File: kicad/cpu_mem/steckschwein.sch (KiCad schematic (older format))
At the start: 28 parts, among them P1 CONN_02X04, P3 CONN_01X03, P4 CONN_02X02, SW1 SW_PUSH, U1 W65C02SP, U2 LM555N, U3 74HCT00, U4 74LS393, U6 28C256, U7 HM62256BLP-7, U8 HM62256BLP-7, X1 OSC

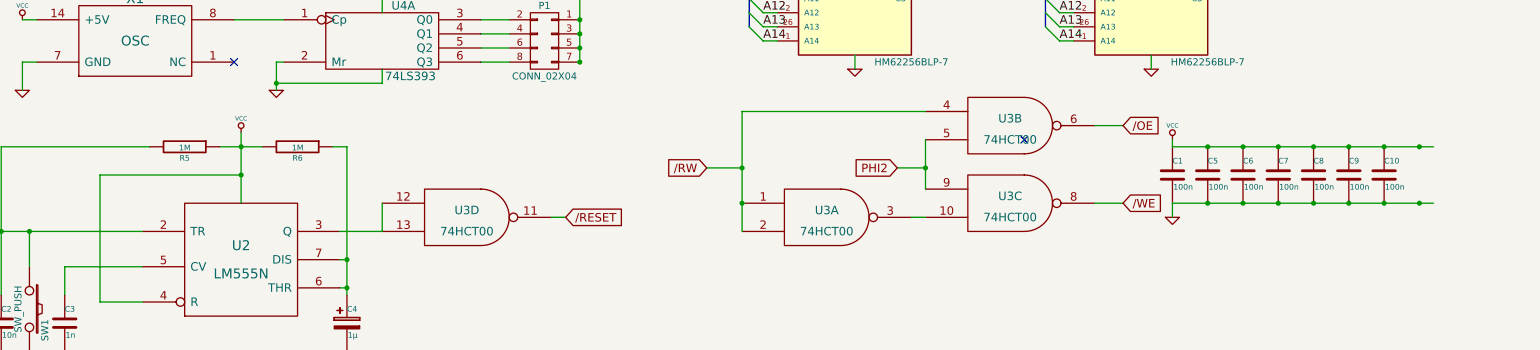
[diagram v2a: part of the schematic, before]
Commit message: memctl register auslesbar
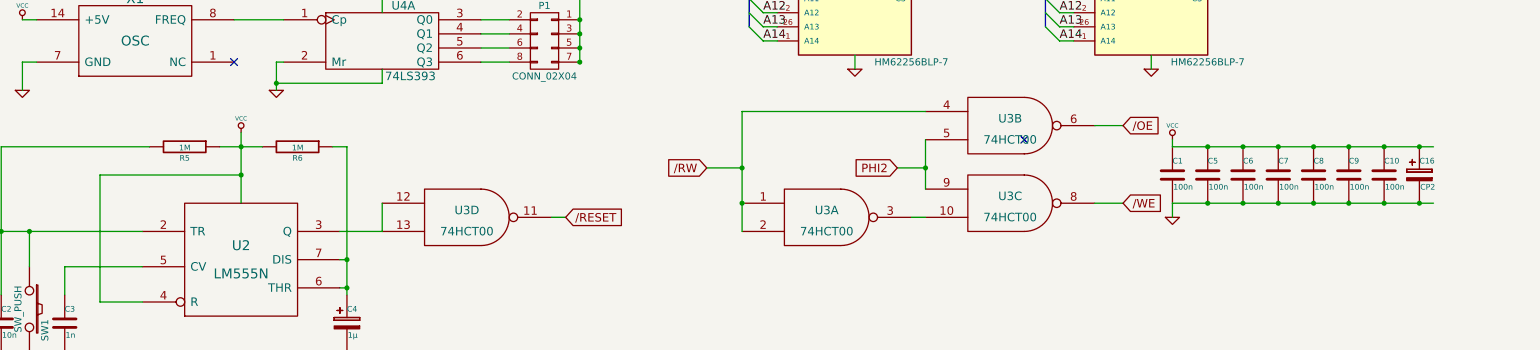
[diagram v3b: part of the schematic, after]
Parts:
- added C16: CP2, Capacitors_Elko_ThroughHole:Elko_vert_11.2x7.5mm_RM2.5, symbol CP2
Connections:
- net GND: now also C16.2
- net VCC: now also C16.1
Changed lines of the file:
@@
 LIBS:74xgxx
 LIBS:ttl_ieee
+LIBS:steckschwein-cache
 EELAYER 24 0
 EELAYER END
@@
 $EndComp
 $Comp
-L VCC #PWR20
+L VCC #PWR01
 U 1 1 5413678B
 P 8900 5600
-F 0 "#PWR20" H 8900 5700 30  0001 C CNN
+F 0 "#PWR01" H 8900 5700 30  0001 C CNN
 F 1 "VCC" H 8900 5700 30  0000 C CNN
 F 2 "" H 8900 5600 60  0000 C CNN
@@
 $EndComp
 $Comp
-L GND #PWR21
+L GND #PWR02
 U 1 1 541367AD
 P 8900 6150
-F 0 "#PWR21" H 8900 6150 30  0001 C CNN
+F 0 "#PWR02" H 8900 6150 30  0001 C CNN
 F 1 "GND" H 8900 6080 30  0001 C CNN
 F 2 "" H 8900 6150 60  0000 C CNN
@@
 $EndComp
 $Comp
-L VCC #PWR6
+L VCC #PWR03
 U 1 1 54136970
 P 2750 2700
-F 0 "#PWR6" H 2750 2800 30  0001 C CNN
+F 0 "#PWR03" H 2750 2800 30  0001 C CNN
 F 1 "VCC" H 2750 2800 30  0000 C CNN
 F 2 "" H 2750 2700 60  0000 C CNN
@@
 $EndComp
 $Comp
-L GND #PWR7
+L GND #PWR04
 U 1 1 541369C9
 P 2750 3250
-F 0 "#PWR7" H 2750 3250 30  0001 C CNN
+F 0 "#PWR04" H 2750 3250 30  0001 C CNN
 F 1 "GND" H 2750 3180 30  0001 C CNN
 F 2 "" H 2750 3250 60  0000 C CNN
@@
 $EndComp
 $Comp
-L VCC #PWR4
+L VCC #PWR05
 U 1 1 54136DD8
 P 2300 5550
-F 0 "#PWR4" H 2300 5650 30  0001 C CNN
+F 0 "#PWR05" H 2300 5650 30  0001 C CNN
 F 1 "VCC" H 2300 5650 30  0000 C CNN
 F 2 "" H 2300 5550 60  0000 C CNN
@@
 $EndComp
 $Comp
-L GND #PWR8
+L GND #PWR06
 U 1 1 541371BF
 P 3050 7400
-F 0 "#PWR8" H 3050 7400 30  0001 C CNN
+F 0 "#PWR06" H 3050 7400 30  0001 C CNN
 F 1 "GND" H 3050 7330 30  0001 C CNN
 F 2 "" H 3050 7400 60  0000 C CNN
@@
 $EndComp
 $Comp
-L VCC #PWR1
+L VCC #PWR07
 U 1 1 5413551C
 P 550 3350
-F 0 "#PWR1" H 550 3450 30  0001 C CNN
+F 0 "#PWR07" H 550 3450 30  0001 C CNN
 F 1 "VCC" H 550 3450 30  0000 C CNN
 F 2 "" H 550 3350 60  0000 C CNN
@@
 $EndComp
 $Comp
-L VCC #PWR11
+L VCC #PWR08
 U 1 1 5413558F
 P 3750 3550
-F 0 "#PWR11" H 3750 3650 30  0001 C CNN
+F 0 "#PWR08" H 3750 3650 30  0001 C CNN
 F 1 "VCC" H 3750 3650 30  0000 C CNN
 F 2 "" H 3750 3550 60  0000 C CNN
@@
 $EndComp
 $Comp
-L VCC #PWR2
+L VCC #PWR09
 U 1 1 54136377
 P 750 4750
-F 0 "#PWR2" H 750 4850 30  0001 C CNN
+F 0 "#PWR09" H 750 4850 30  0001 C CNN
 F 1 "VCC" H 750 4850 30  0000 C CNN
 F 2 "" H 750 4750 60  0000 C CNN
@@
 $EndComp
 $Comp
-L GND #PWR3
+L GND #PWR010
 U 1 1 541363D2
 P 750 5250
-F 0 "#PWR3" H 750 5250 30  0001 C CNN
+F 0 "#PWR010" H 750 5250 30  0001 C CNN
 F 1 "GND" H 750 5180 30  0001 C CNN
 F 2 "" H 750 5250 60  0000 C CNN
@@
 $EndComp
 $Comp
-L GND #PWR5
+L GND #PWR011
 U 1 1 5413653F
 P 2550 5250
-F 0 "#PWR5" H 2550 5250 30  0001 C CNN
+F 0 "#PWR011" H 2550 5250 30  0001 C CNN
 F 1 "GND" H 2550 5180 30  0001 C CNN
 F 2 "" H 2550 5250 60  0000 C CNN
@@
 $EndComp
 $Comp
-L VCC #PWR9
+L VCC #PWR012
 U 1 1 5413674B
 P 3300 4550
-F 0 "#PWR9" H 3300 4650 30  0001 C CNN
+F 0 "#PWR012" H 3300 4650 30  0001 C CNN
 F 1 "VCC" H 3300 4650 30  0000 C CNN
 F 2 "" H 3300 4550 60  0000 C CNN
@@
 $EndComp
 $Comp
-L VCC #PWR14
+L VCC #PWR013
 U 1 1 5413EA26
 P 7000 2550
-F 0 "#PWR14" H 7000 2650 30  0001 C CNN
+F 0 "#PWR013" H 7000 2650 30  0001 C CNN
 F 1 "VCC" H 7000 2650 30  0000 C CNN
 F 2 "" H 7000 2550 60  0000 C CNN
@@
 $EndComp
 $Comp
-L GND #PWR10
+L GND #PWR014
 U 1 1 5414A44F
 P 3400 3450
-F 0 "#PWR10" H 3400 3450 30  0001 C CNN
+F 0 "#PWR014" H 3400 3450 30  0001 C CNN
 F 1 "GND" H 3400 3380 30  0001 C CNN
 F 2 "" H 3400 3450 60  0000 C CNN
@@
 A5
 $Comp
-L VCC #PWR16
+L VCC #PWR015
 U 1 1 543745A2
 P 8100 700
-F 0 "#PWR16" H 8100 800 30  0001 C CNN
+F 0 "#PWR015" H 8100 800 30  0001 C CNN
 F 1 "VCC" H 8100 800 30  0000 C CNN
 F 2 "" H 8100 700 60  0000 C CNN
@@
 $EndComp
 $Comp
-L GND #PWR17
+L GND #PWR016
 U 1 1 543748B3
 P 8100 3000
-F 0 "#PWR17" H 8100 3000 30  0001 C CNN
+F 0 "#PWR016" H 8100 3000 30  0001 C CNN
 F 1 "GND" H 8100 2930 30  0001 C CNN
 F 2 "" H 8100 3000 60  0000 C CNN
@@
 $EndComp
 $Comp
-L VCC #PWR12
+L VCC #PWR017
 U 1 1 54374D46
 P 6650 3300
-F 0 "#PWR12" H 6650 3400 30  0001 C CNN
+F 0 "#PWR017" H 6650 3400 30  0001 C CNN
 F 1 "VCC" H 6650 3400 30  0000 C CNN
 F 2 "" H 6650 3300 60  0000 C CNN
@@
 $EndComp
 $Comp
-L VCC #PWR18
+L VCC #PWR018
 U 1 1 54374E0E
 P 8750 3300
-F 0 "#PWR18" H 8750 3400 30  0001 C CNN
+F 0 "#PWR018" H 8750 3400 30  0001 C CNN
 F 1 "VCC" H 8750 3400 30  0000 C CNN
 F 2 "" H 8750 3300 60  0000 C CNN
@@
 $EndComp
 $Comp
-L GND #PWR13
+L GND #PWR019
 U 1 1 54375105
 P 6650 5100
-F 0 "#PWR13" H 6650 5100 30  0001 C CNN
+F 0 "#PWR019" H 6650 5100 30  0001 C CNN
 F 1 "GND" H 6650 5030 30  0001 C CNN
 F 2 "" H 6650 5100 60  0000 C CNN
@@
 $EndComp
 $Comp
-L GND #PWR19
+L GND #PWR020
 U 1 1 54375267
 P 8750 5100
-F 0 "#PWR19" H 8750 5100 30  0001 C CNN
+F 0 "#PWR020" H 8750 5100 30  0001 C CNN
 F 1 "GND" H 8750 5030 30  0001 C CNN
 F 2 "" H 8750 5100 60  0000 C CNN
@@
 	1300 6750 1300 5850
 Wire Wire Line
-	1300 5850 2300 5850
+	2300 5850 1300 5850
 Connection ~ 2300 5850
 Wire Wire Line
@@
 Wire Wire Line
 	6100 1950 4850 1950
+$Comp
+L CP2 C16
+U 1 1 546AA0E1
+P 10650 5850
+F 0 "C16" H 10650 5950 40  0000 L CNN
+F 1 "CP2" H 10656 5765 40  0000 L CNN
+F 2 "Capacitors_Elko_ThroughHole:Elko_vert_11.2x7.5mm_RM2.5" H 10688 5700 30  0001 C CNN
+F 3 "" H 10650 5850 60  0000 C CNN
+	1    10650 5850
+	1    0    0    -1
+$EndComp
 $EndSCHEMATC

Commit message: update
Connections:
- net /CS_ROM: now also U6.20 (CS)
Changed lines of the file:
@@
 LIBS:ttl_ieee
 LIBS:steckschwein-cache
-EELAYER 24 0
+EELAYER 25 0
 EELAYER END
 $Descr A4 11693 8268
@@
 	1300 6750 1300 5850
 Wire Wire Line
-	2300 5850 1300 5850
+	1300 5850 2300 5850
 Connection ~ 2300 5850
 Wire Wire Line
@@
 Wire Wire Line
 	7400 2750 7200 2750
-Wire Wire Line
-	7400 2850 7200 2850
 Wire Bus Line
 	9050 750  9050 1650
@@
 Text Label 9450 4600 0    60   ~ 0
 /CS_HIRAM
-Text Label 7000 2950 0    60   ~ 0
-/CS_ROM
-Wire Wire Line
-	4850 800  5150 800
 Wire Wire Line
 	4850 900  5150 900
 Wire Wire Line
 	4850 1000 5150 1000
-Text Label 5100 800  0    60   ~ 0
-/CS_ROM
 Text Label 5100 900  0    60   ~ 0
 /CS_LORAM
@@
 	1    0    0    -1
 $EndComp
+Wire Wire Line
+	6300 2850 7400 2850
+Text Label 6950 2950 0    60   ~ 0
+/CS_ROM
+Wire Wire Line
+	4850 800  6300 800
+Text Label 5150 800  0    60   ~ 0
+/CS_ROM
+Wire Wire Line
+	6300 800  6300 2850
 $EndSCHEMATC

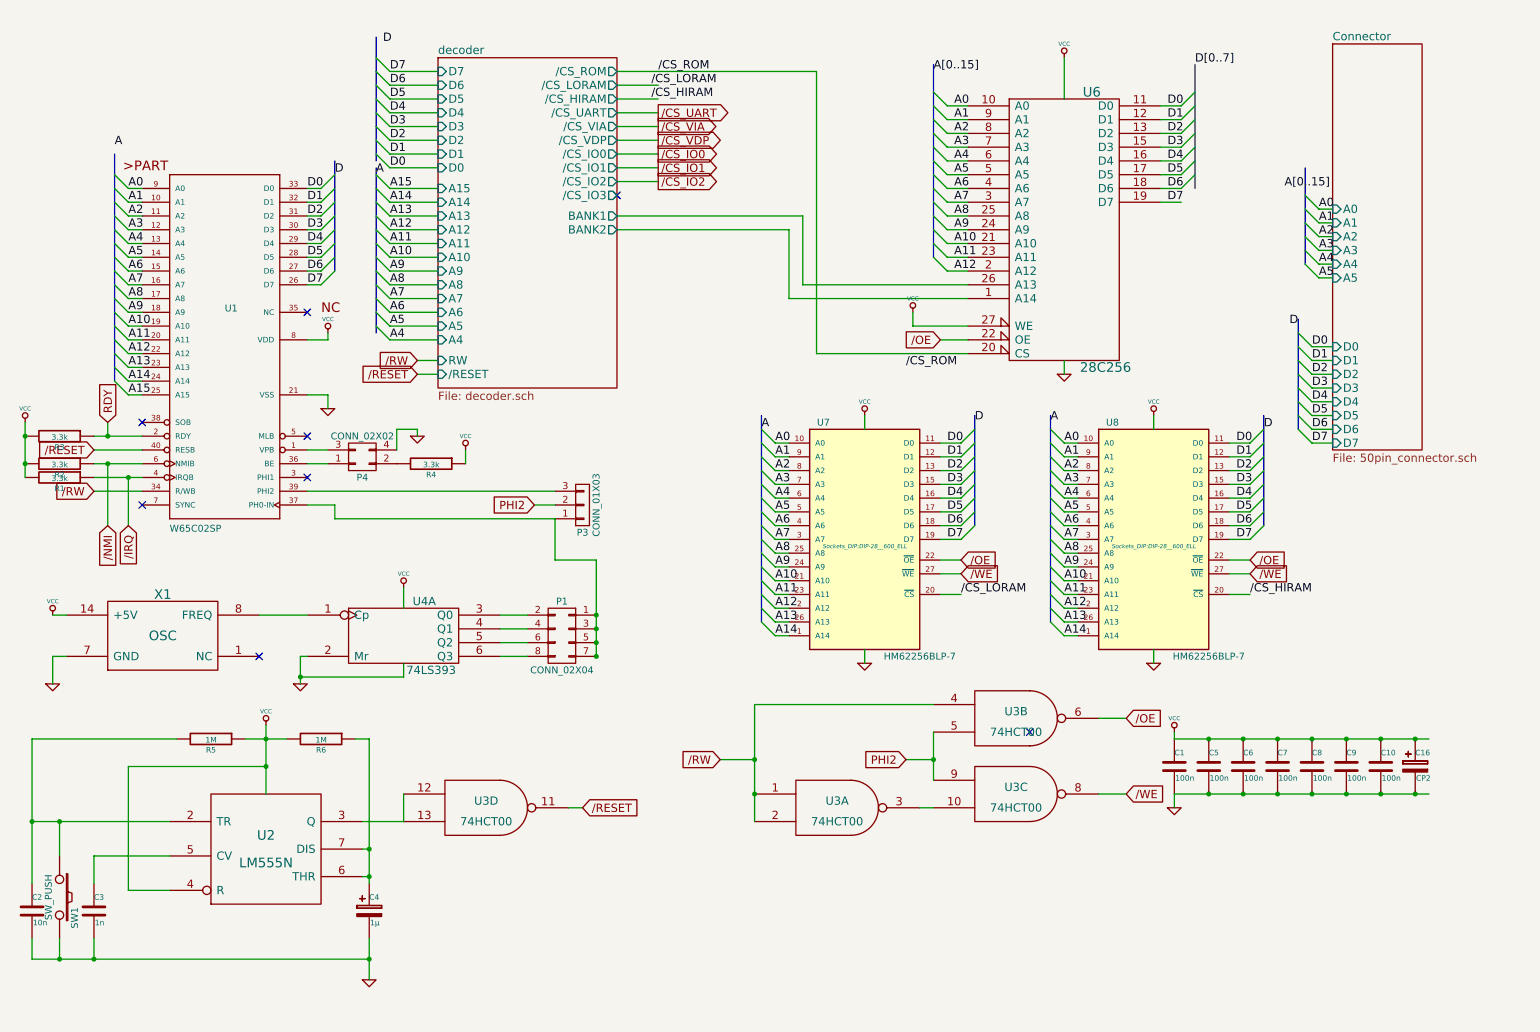
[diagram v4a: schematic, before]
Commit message: anpassungen latch, decoder, 2. unit 393 inputs auf masse
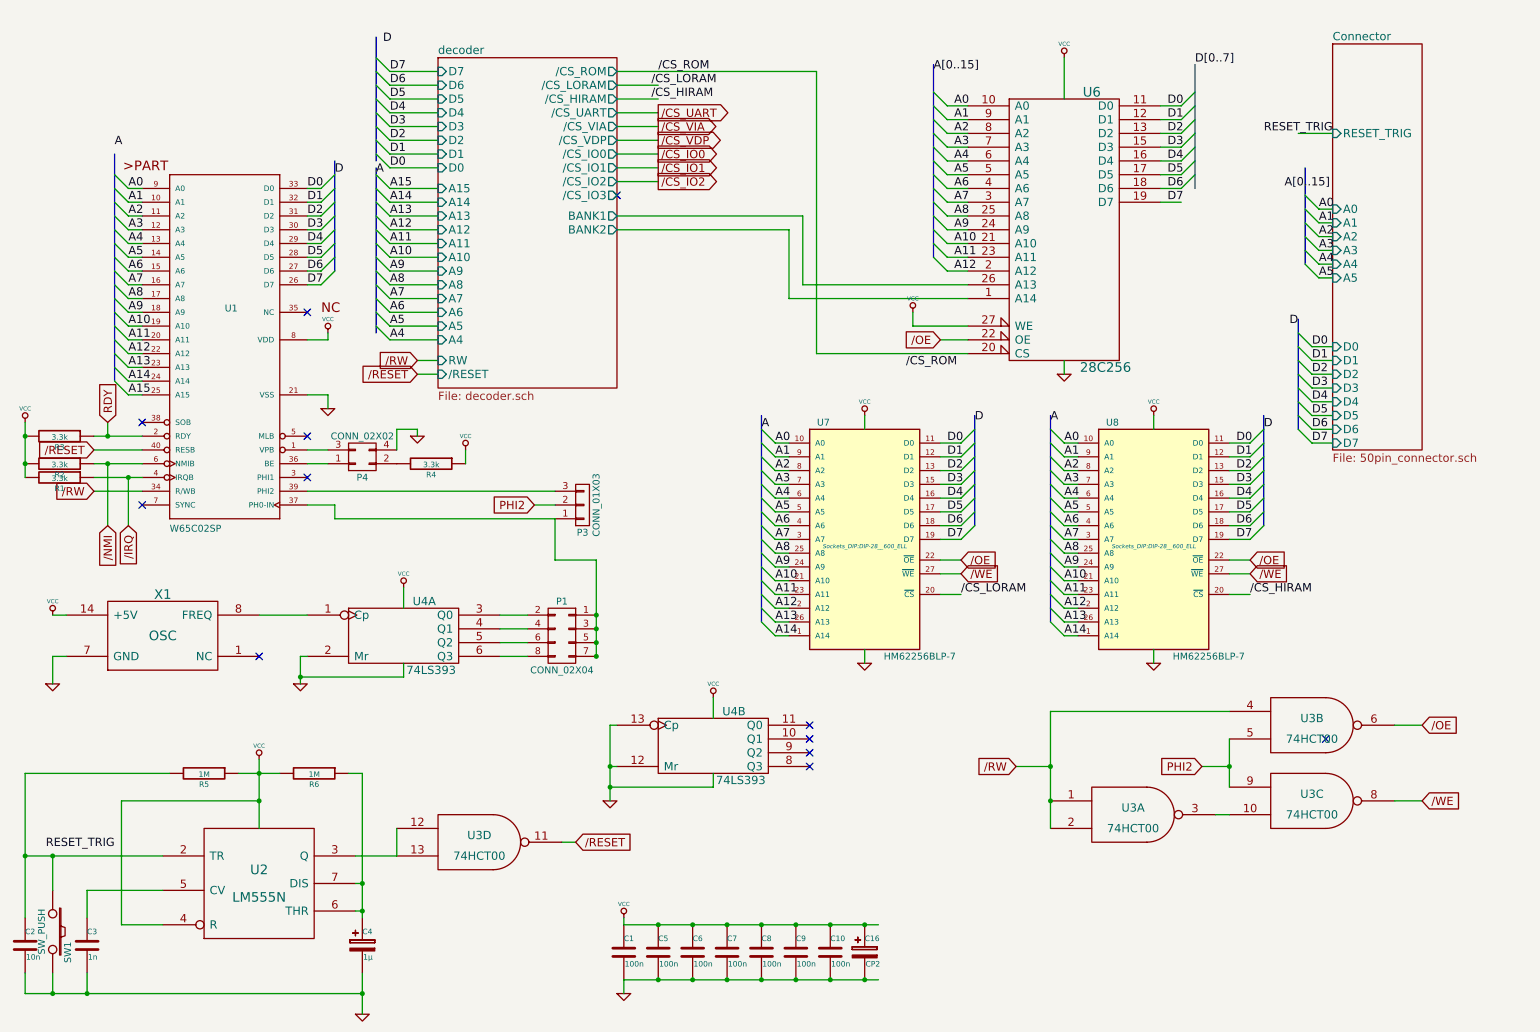
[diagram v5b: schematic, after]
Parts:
- added unit 2 of U4
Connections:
- net GND: now also U4.12 (Mr), U4.13 (Cp), U4.7 (GND)
- net VCC: now also U4.14 (VCC)
- no-connect marks 8 -> 12
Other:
- moved on the sheet: C1, C10, C16, C2, C3, C4, C5, C6, C7, C8, C9, R5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

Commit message: reset_trig, letzte ratsline fix
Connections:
- net RESET_TRIG: now also C2.1, R5.2, SW1.1, U2.2 (TR)
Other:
- moved on the sheet: C2, SW1
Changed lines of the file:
@@
 L C C2
 U 1 1 54137610
-P 550 7150
-F 0 "C2" H 550 7250 40  0000 L CNN
-F 1 "10n" H 556 7065 40  0000 L CNN
-F 2 "Discret:C1" H 588 7000 30  0001 C CNN
-F 3 "" H 550 7150 60  0000 C CNN
-	1    550  7150
+P 800 7150
+F 0 "C2" H 800 7250 40  0000 L CNN
+F 1 "10n" H 806 7065 40  0000 L CNN
+F 2 "Discret:C1" H 838 7000 30  0001 C CNN
+F 3 "" H 800 7150 60  0000 C CNN
+	1    800  7150
 	1    0    0    -1
 $EndComp
@@
 L SW_PUSH SW1
 U 1 1 54147B44
-P 750 7050
-F 0 "SW1" H 900 7160 50  0000 C CNN
-F 1 "SW_PUSH" H 750 6970 50  0000 C CNN
-F 2 "Discret:PUSH_BUTT_SHAPE1" H 750 7050 60  0001 C CNN
-F 3 "" H 750 7050 60  0000 C CNN
-	1    750  7050
+P 3200 7150
+F 0 "SW1" H 3350 7260 50  0000 C CNN
+F 1 "SW_PUSH" H 3200 7070 50  0000 C CNN
+F 2 "Discret:PUSH_BUTT_SHAPE1" H 3200 7150 60  0001 C CNN
+F 3 "" H 3200 7150 60  0000 C CNN
+	1    3200 7150
 	0    1    1    0
 $EndComp
@@
 L VCC #PWR015
 U 1 1 543745A2
-P 8100 700
-F 0 "#PWR015" H 8100 800 30  0001 C CNN
-F 1 "VCC" H 8100 800 30  0000 C CNN
-F 2 "" H 8100 700 60  0000 C CNN
-F 3 "" H 8100 700 60  0000 C CNN
-	1    8100 700
+P 8100 850
+F 0 "#PWR015" H 8100 950 30  0001 C CNN
+F 1 "VCC" H 8100 950 30  0000 C CNN
+F 2 "" H 8100 850 60  0000 C CNN
+F 3 "" H 8100 850 60  0000 C CNN
+	1    8100 850
 	1    0    0    -1
 $EndComp
@@
 Connection ~ 2250 6100
 Wire Wire Line
-	550  5900 1600 5900
-Wire Wire Line
-	550  5900 550  6950
-Wire Wire Line
-	550  6500 1550 6500
-Connection ~ 550  6500
+	800  5900 1600 5900
+Wire Wire Line
+	800  5900 800  6950
+Wire Wire Line
+	500  6500 1550 6500
+Connection ~ 800  6500
 Wire Wire Line
 	1550 6750 1000 6750
@@
 	1000 6750 1000 6950
 Wire Wire Line
-	550  7350 550  7500
-Wire Wire Line
-	550  7500 3000 7500
+	800  7350 800  7500
+Wire Wire Line
+	800  7500 3000 7500
 Wire Wire Line
 	1000 7350 1000 7500
@@
 Connection ~ 6400 7400
 Connection ~ 6150 7400
-Wire Wire Line
-	750  6750 750  6500
-Connection ~ 750  6500
-Wire Wire Line
-	750  7350 750  7500
-Connection ~ 750  7500
 Wire Bus Line
 	8000 3300 8000 4800
@@
 	9950 2300 10050 2300
 Wire Wire Line
-	8100 700  8100 1000
-Wire Wire Line
 	8100 3000 8100 2900
-Wire Wire Line
-	6650 3300 6650 3400
-Wire Wire Line
-	8750 3300 8750 3400
 Wire Wire Line
 	6650 5000 6650 5100
@@
 NoConn ~ 6250 5750
 NoConn ~ 6250 5850
-Text Label 700  6450 0    60   ~ 0
-RESET_TRIG
-Wire Wire Line
-	10050 1250 9800 1250
+Wire Wire Line
+	10050 1250 9550 1250
 Text Label 9550 1250 0    60   ~ 0
 RESET_TRIG
+Text Label 500  6500 0    60   ~ 0
+RESET_TRIG
+$Comp
+L GND #PWR023
+U 1 1 54B14888
+P 3200 7650
+F 0 "#PWR023" H 3200 7650 30  0001 C CNN
+F 1 "GND" H 3200 7580 30  0001 C CNN
+F 2 "" H 3200 7650 60  0000 C CNN
+F 3 "" H 3200 7650 60  0000 C CNN
+	1    3200 7650
+	1    0    0    -1
+$EndComp
+Wire Wire Line
+	3200 7450 3200 7650
+Wire Wire Line
+	3200 6850 3200 6600
+Text Label 3200 6700 0    60   ~ 0
+RESET_TRIG
+Wire Wire Line
+	6650 3300 6650 3400
+Wire Wire Line
+	8100 850  8100 1000
+Wire Wire Line
+	8750 3300 8750 3400
 $EndSCHEMATC

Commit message: power anschluss
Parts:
- added P6: POWER, Pin_Headers:Pin_Header_Angled_1x04, symbol CONN_01X04
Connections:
- wire segments 241 -> 246
- no-connect marks 12 -> 13
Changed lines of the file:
@@
 Wire Wire Line
 	8750 3300 8750 3400
+$Comp
+L CONN_01X04 P6
+U 1 1 54B57D9B
+P 2300 950
+F 0 "P6" H 2300 1200 50  0000 C CNN
+F 1 "POWER" V 2400 950 50  0000 C CNN
+F 2 "Pin_Headers:Pin_Header_Angled_1x04" H 2300 950 60  0001 C CNN
+F 3 "" H 2300 950 60  0000 C CNN
+	1    2300 950
+	1    0    0    1
+$EndComp
+$Comp
+L VCC #PWR024
+U 1 1 54B581D7
+P 2050 700
+F 0 "#PWR024" H 2050 800 30  0001 C CNN
+F 1 "VCC" H 2050 800 30  0000 C CNN
+F 2 "" H 2050 700 60  0000 C CNN
+F 3 "" H 2050 700 60  0000 C CNN
+	1    2050 700
+	1    0    0    -1
+$EndComp
+$Comp
+L GND #PWR025
+U 1 1 54B5858D
+P 2050 1250
+F 0 "#PWR025" H 2050 1250 30  0001 C CNN
+F 1 "GND" H 2050 1180 30  0001 C CNN
+F 2 "" H 2050 1250 60  0000 C CNN
+F 3 "" H 2050 1250 60  0000 C CNN
+	1    2050 1250
+	1    0    0    -1
+$EndComp
+Wire Wire Line
+	2100 900  2050 900
+Wire Wire Line
+	2050 900  2050 1250
+Wire Wire Line
+	2050 700  2050 800
+Wire Wire Line
+	2050 800  2100 800
+Wire Wire Line
+	2100 1000 2050 1000
+Connection ~ 2050 1000
+NoConn ~ 2100 1100
 $EndSCHEMATC

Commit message: blinkenlights
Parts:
- added D1, D2, D3: LED, LEDs:LED-3MM, symbol LED
- added R7, R8, R9: 270, Discret:R3, symbol R
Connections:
- wire segments 246 -> 253
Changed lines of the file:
@@
 Connection ~ 2050 1000
 NoConn ~ 2100 1100
+$Comp
+L LED D1
+U 1 1 54C38B5D
+P 5700 2250
+F 0 "D1" H 5700 2350 50  0000 C CNN
+F 1 "LED" H 5700 2150 50  0000 C CNN
+F 2 "LEDs:LED-3MM" H 5700 2250 60  0001 C CNN
+F 3 "" H 5700 2250 60  0000 C CNN
+	1    5700 2250
+	1    0    0    -1
+$EndComp
+$Comp
+L LED D2
+U 1 1 54C38C62
+P 5700 2550
+F 0 "D2" H 5700 2650 50  0000 C CNN
+F 1 "LED" H 5700 2450 50  0000 C CNN
+F 2 "LEDs:LED-3MM" H 5700 2550 60  0001 C CNN
+F 3 "" H 5700 2550 60  0000 C CNN
+	1    5700 2550
+	1    0    0    -1
+$EndComp
+$Comp
+L LED D3
+U 1 1 54C38D3E
+P 5700 2850
+F 0 "D3" H 5700 2950 50  0000 C CNN
+F 1 "LED" H 5700 2750 50  0000 C CNN
+F 2 "LEDs:LED-3MM" H 5700 2850 60  0001 C CNN
+F 3 "" H 5700 2850 60  0000 C CNN
+	1    5700 2850
+	1    0    0    -1
+$EndComp
+$Comp
+L R R7
+U 1 1 54C39594
+P 5200 2250
+F 0 "R7" V 5280 2250 40  0000 C CNN
+F 1 "270" V 5207 2251 40  0000 C CNN
+F 2 "Discret:R3" V 5130 2250 30  0001 C CNN
+F 3 "" H 5200 2250 30  0000 C CNN
+	1    5200 2250
+	0    1    1    0
+$EndComp
+$Comp
+L R R8
+U 1 1 54C3A498
+P 5200 2550
+F 0 "R8" V 5280 2550 40  0000 C CNN
+F 1 "270" V 5207 2551 40  0000 C CNN
+F 2 "Discret:R3" V 5130 2550 30  0001 C CNN
+F 3 "" H 5200 2550 30  0000 C CNN
+	1    5200 2550
+	0    1    1    0
+$EndComp
+$Comp
+L R R9
+U 1 1 54C3A4DF
+P 5200 2850
+F 0 "R9" V 5280 2850 40  0000 C CNN
+F 1 "270" V 5207 2851 40  0000 C CNN
+F 2 "Discret:R3" V 5130 2850 30  0001 C CNN
+F 3 "" H 5200 2850 30  0000 C CNN
+	1    5200 2850
+	0    1    1    0
+$EndComp
+Wire Wire Line
+	4950 2100 4950 2850
+$Comp
+L VCC #PWR026
+U 1 1 54C3BFBB
+P 4950 2100
+F 0 "#PWR026" H 4950 2200 30  0001 C CNN
+F 1 "VCC" H 4950 2200 30  0000 C CNN
+F 2 "" H 4950 2100 60  0000 C CNN
+F 3 "" H 4950 2100 60  0000 C CNN
+	1    4950 2100
+	1    0    0    -1
+$EndComp
+Connection ~ 4950 2250
+Wire Wire Line
+	5450 2250 5500 2250
+Wire Wire Line
+	5450 2550 5500 2550
+Wire Wire Line
+	5450 2850 5500 2850
+Wire Wire Line
+	5900 2250 6050 2250
+Wire Wire Line
+	5900 2550 6050 2550
+Wire Wire Line
+	5900 2850 6050 2850
+Text Label 6000 2250 0    60   ~ 0
+/CS_ROM
+Text Label 6000 2550 0    60   ~ 0
+/CS_LORAM
+Text Label 6000 2850 0    60   ~ 0
+/CS_HIRAM
+Connection ~ 4950 2550
+Connection ~ 4950 2850
 $EndSCHEMATC
